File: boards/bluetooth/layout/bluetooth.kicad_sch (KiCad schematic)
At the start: 10 parts, among them U1 HM-19

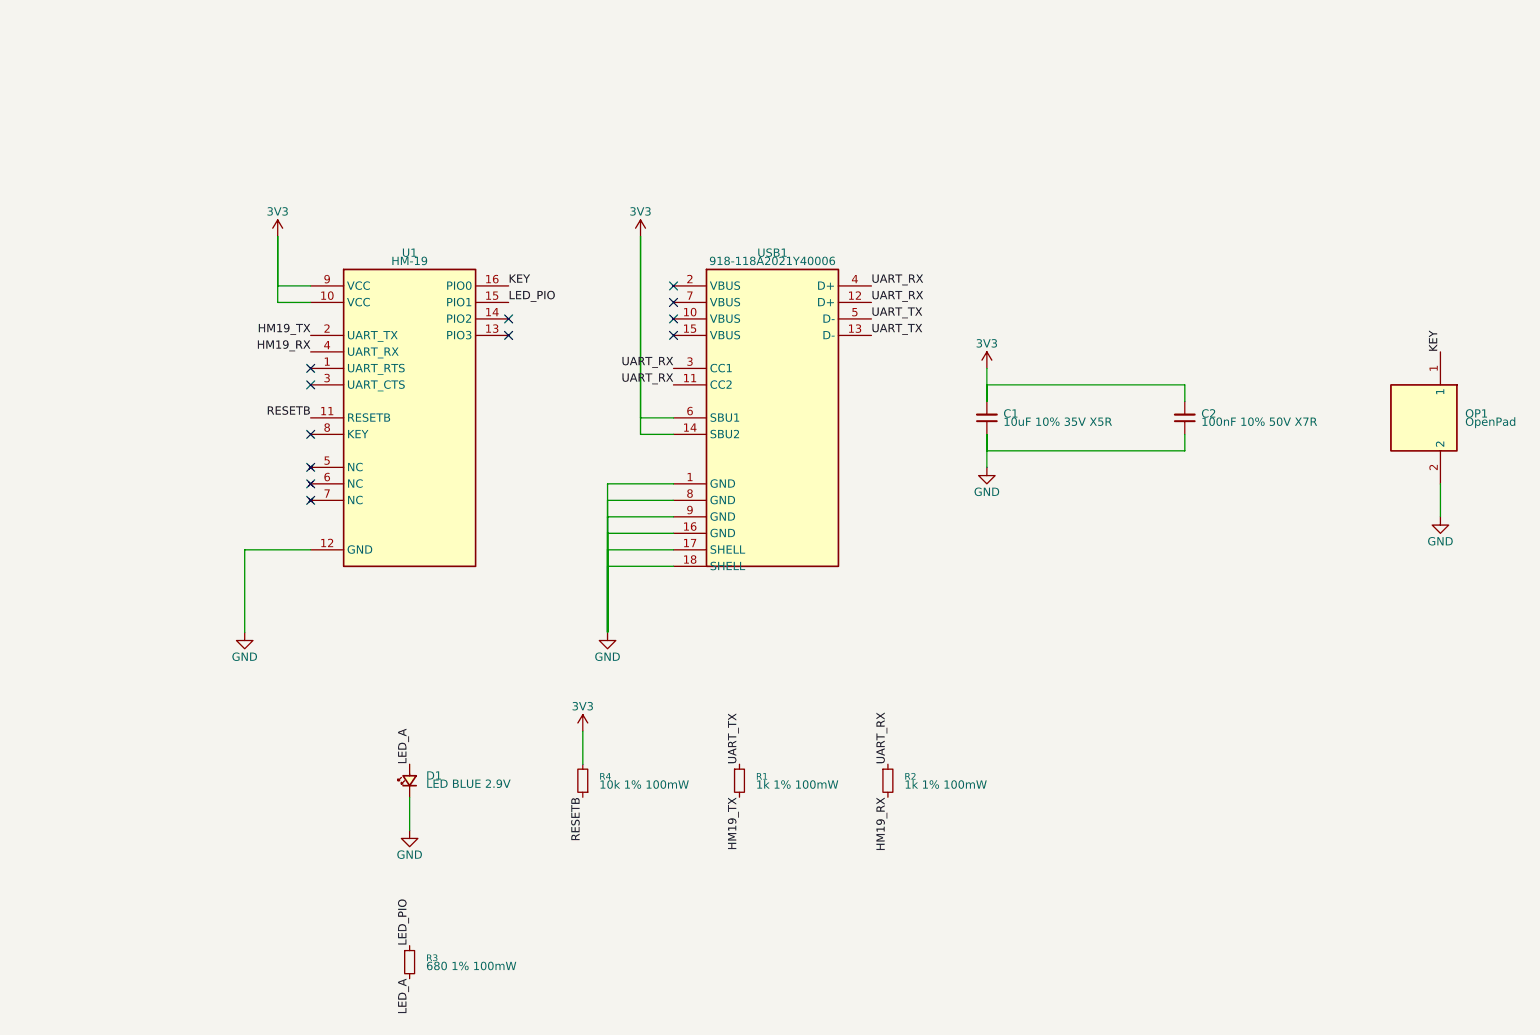
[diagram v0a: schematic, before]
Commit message: ✨ Place the schematics from per-sheet placement files
micras-pcb sch redraws each sheet pcb apply writes from
boards/<board>/schematic/<sheet>.toml: parts, wires, labels, power
symbols, titled frames, paper and title block, the root's sheet
symbols, and a ports column for the module sheets' extra labels. It
fails unless KiCad's netlist of the placed schematic equals pcb's.
make gen runs it after pcb apply; make check's sch gate fails on a part
without a placement, and tests/test_placement.py on any overlap.

The encoder and Bluetooth sheets are placed; the main board's DRIVERS
sheet is drafted.
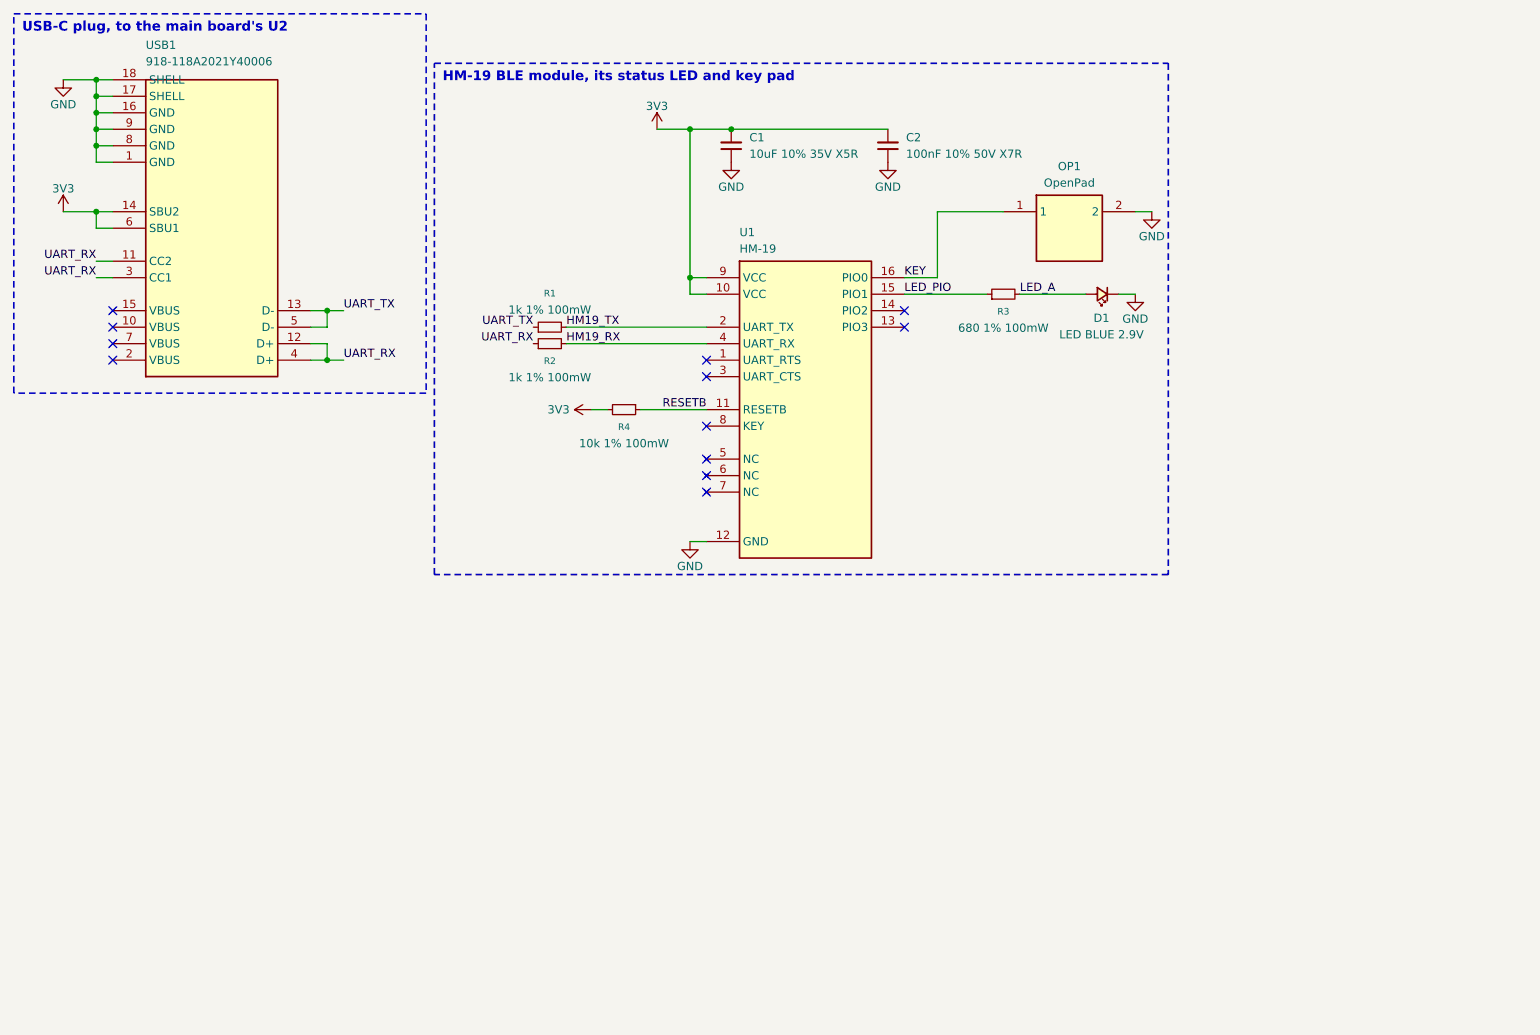
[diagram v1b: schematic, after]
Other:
- note added: "HM-19 BLE module, its status LED and key pad"
- note added: "USB-C plug, to the main board's U2"
- title: (none) -> Bluetooth module
- moved on the sheet: C1, C2, D1, OP1, R1, R2, R3, R4, U1, USB1
